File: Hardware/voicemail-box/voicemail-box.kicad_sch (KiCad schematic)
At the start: 6 parts, among them J101 Conn_02x08_Odd_Even, J102 Conn_02x03_Odd_Even, J103 Conn_02x08_Odd_Even

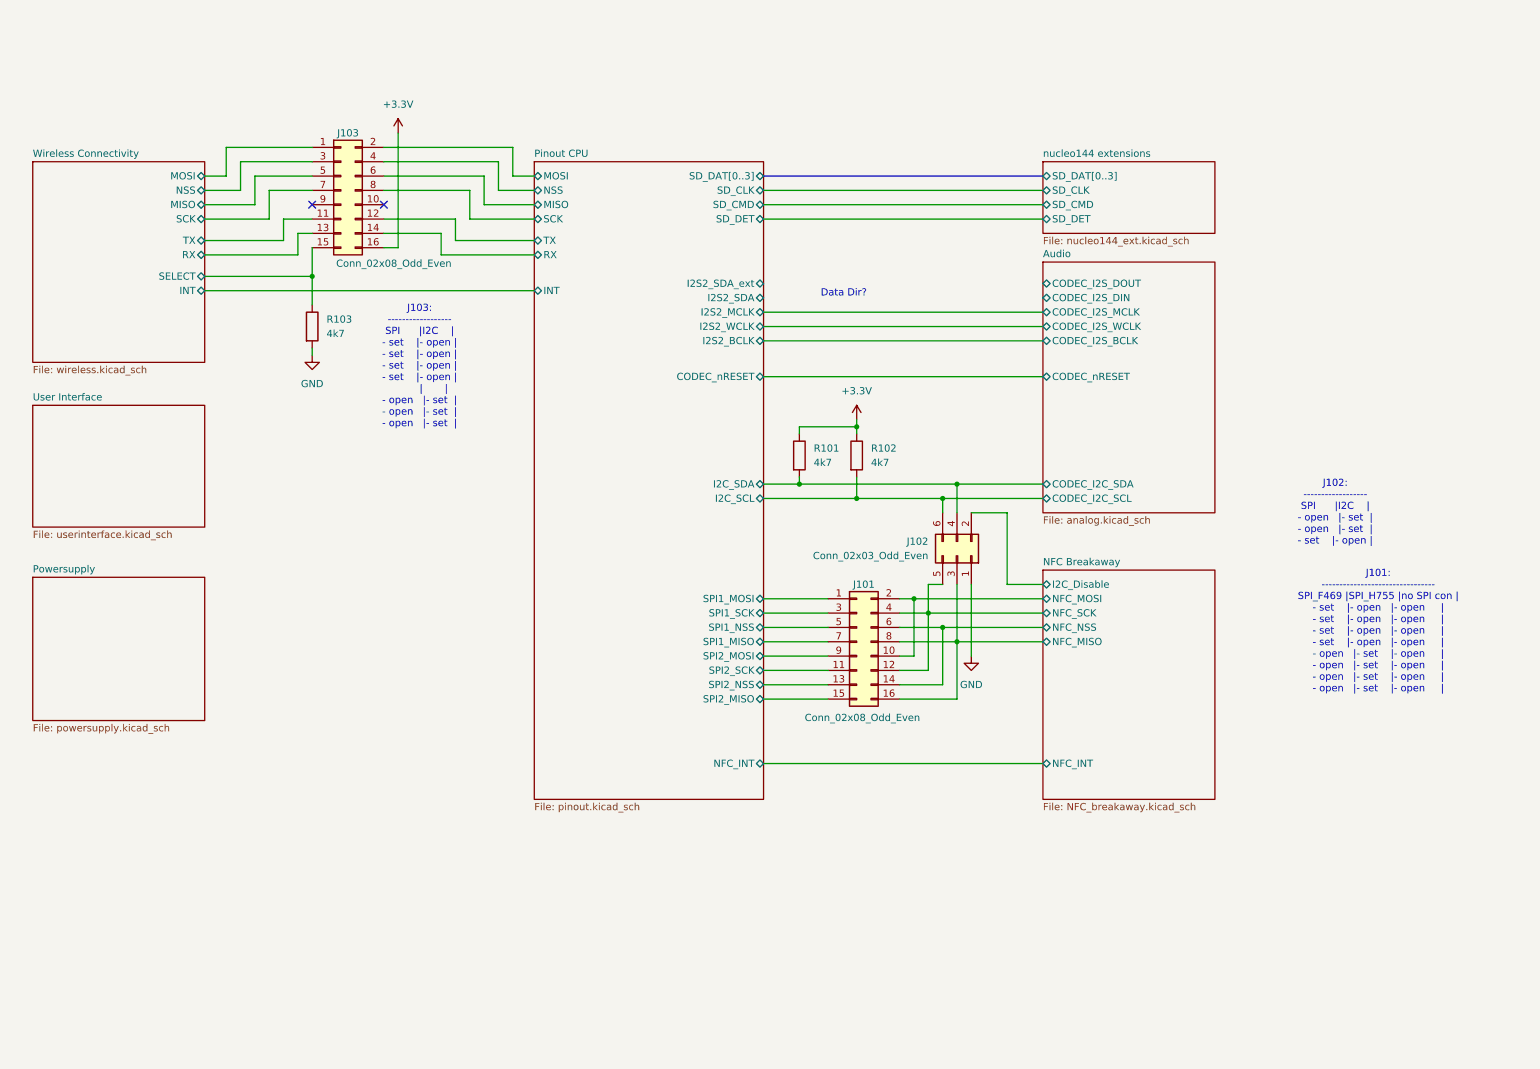
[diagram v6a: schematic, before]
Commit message: HW Layout progress todo: + Antenna + Audio Jacks + Planes (Supply only)
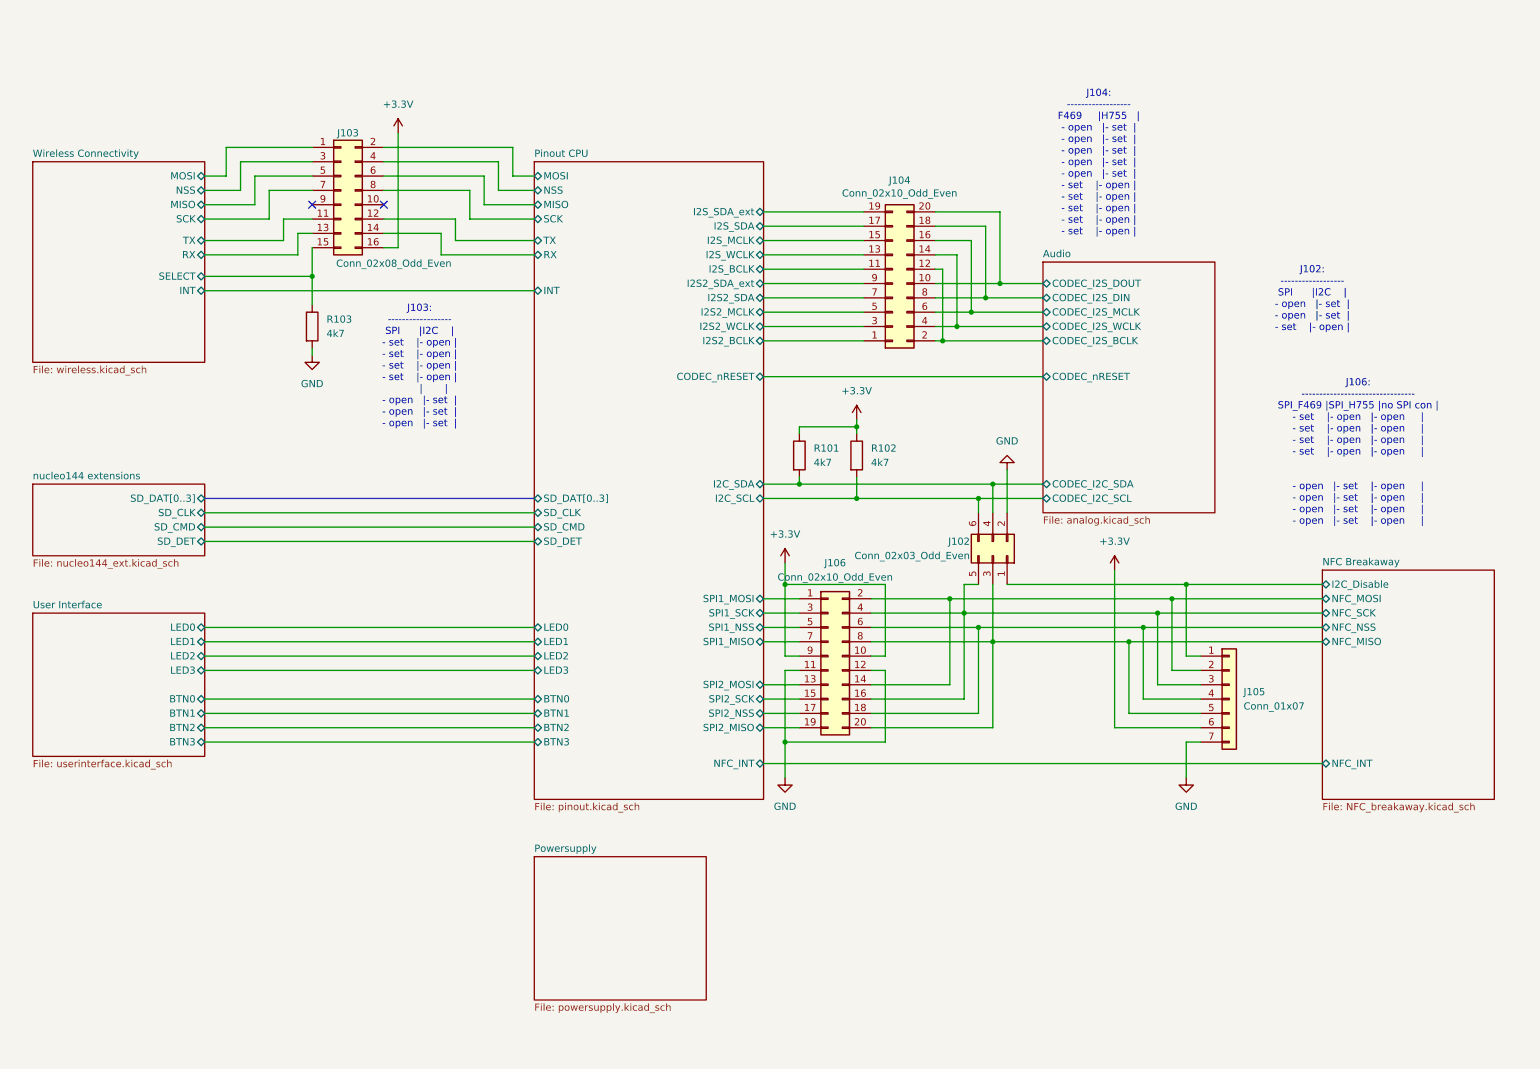
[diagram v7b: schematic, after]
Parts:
- removed J101: Conn_02x08_Odd_Even, Connector_PinHeader_2.54mm:PinHeader_2x08_P2.54mm_Vertical, symbol Connector_Generic:Conn_02x08_Odd_Even
- added J104, J106: Conn_02x10_Odd_Even, Connector_PinHeader_2.54mm:PinHeader_2x10_P2.54mm_Vertical, symbol Connector_Generic:Conn_02x10_Odd_Even
- added J105: Conn_01x07, Connector_PinHeader_2.54mm:PinHeader_1x07_P2.54mm_Vertical, symbol Connector_Generic:Conn_01x07
- J102: footprint Connector_PinSocket_2.54mm:PinSocket_2x03_P2.54mm_Vertical -> Connector_PinHeader_2.54mm:PinHeader_2x03_P2.54mm_Vertical
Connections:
- net +3.3V: now also J105.6 (Pin_6), J106.10 (Pin_10), J106.9 (Pin_9)
- net Audio/CODEC_I2S_BCLK: now also J104.12 (Pin_12), J104.2 (Pin_2)
- net Audio/CODEC_I2S_DIN: now also J104.18 (Pin_18), J104.8 (Pin_8)
- net Audio/CODEC_I2S_DOUT: now also J104.10 (Pin_10), J104.20 (Pin_20)
- net Audio/CODEC_I2S_MCLK: now also J104.16 (Pin_16), J104.6 (Pin_6)
- net Audio/CODEC_I2S_WCLK: now also J104.14 (Pin_14), J104.4 (Pin_4)
- net GND: now also J102.2 (Pin_2), J105.7 (Pin_7), J106.11 (Pin_11), J106.12 (Pin_12); no longer J102.1 (Pin_1)
- net NFC Breakaway/I2C_Disable: now also J102.1 (Pin_1), J105.1 (Pin_1); no longer J102.2 (Pin_2)
- net NFC Breakaway/NFC_MISO: now also J105.5 (Pin_5), J106.20 (Pin_20), J106.8 (Pin_8)
- net NFC Breakaway/NFC_MOSI: now also J105.2 (Pin_2), J106.14 (Pin_14), J106.2 (Pin_2)
- net NFC Breakaway/NFC_NSS: now also J105.4 (Pin_4), J106.18 (Pin_18), J106.6 (Pin_6)
- net NFC Breakaway/NFC_SCK: now also J105.3 (Pin_3), J106.16 (Pin_16), J106.4 (Pin_4)
- net Pinout CPU/I2S2_SDA: now also J104.7 (Pin_7)
- net Pinout CPU/I2S2_SDA_ext: now also J104.9 (Pin_9)
- net Pinout CPU/SPI1_MISO: now also J106.7 (Pin_7)
- net Pinout CPU/SPI1_MOSI: now also J106.1 (Pin_1)
- net Pinout CPU/SPI1_NSS: now also J106.5 (Pin_5)
- net Pinout CPU/SPI1_SCK: now also J106.3 (Pin_3)
- net Pinout CPU/SPI2_MISO: now also J106.19 (Pin_19)
- net Pinout CPU/SPI2_MOSI: now also J106.13 (Pin_13)
- net Pinout CPU/SPI2_NSS: now also J106.17 (Pin_17)
- net Pinout CPU/SPI2_SCK: now also J106.15 (Pin_15)
- new net Pinout CPU/I2S2_BCLK: J104.1 (Pin_1)
- new net Pinout CPU/I2S2_MCLK: J104.5 (Pin_5)
- new net Pinout CPU/I2S2_WCLK: J104.3 (Pin_3)
- new net Pinout CPU/I2S_BCLK: J104.11 (Pin_11)
- new net Pinout CPU/I2S_MCLK: J104.15 (Pin_15)
- new net Pinout CPU/I2S_SDA: J104.17 (Pin_17)
- new net Pinout CPU/I2S_SDA_ext: J104.19 (Pin_19)
- new net Pinout CPU/I2S_WCLK: J104.13 (Pin_13)
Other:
- sheet Pinout CPU ports: added BTN0, BTN1, BTN2, BTN3, I2S_BCLK, I2S_MCLK, I2S_SDA, I2S_SDA_ext, I2S_WCLK, LED0, LED1, LED2, LED3; removed none
- sheet User Interface ports: added BTN0, BTN1, BTN2, BTN3, LED0, LED1, LED2, LED3; removed none
- note added: "J104: ------------------ F469 |H755 | - open |- set | - open |- set | - open |- set | - open |- set | - open |- set | - set |- open | - set |- open | - set |- open | - set |- open | - set |- open |"
- note added: "J106: -------------------------------- SPI_F469 |SPI_H755 |no SPI con | - set |- open |- open | - set |- open |- open | - set |- open |- open | - set |- open |- open | - open |- set |- open | - open |- set |- open | - open |- set |- open | - open |- set |- open |"
- note removed: "Data Dir?"
- note removed: "J101: -------------------------------- SPI_F469 |SPI_H755 |no SPI con | - set |- open |- open | - set |- open |- open | - set |- open |- open | - set |- open |- open | - open |- set |- open | - open |- set |- open | - open |- set |- open | - open |- set |- open |"
- moved on the sheet: J102

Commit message: layout progress step
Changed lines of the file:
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@@
 	(sheet
 		(at 20.32 119.38)
-		(size 30.48 25.4)
+		(size 30.48 41.91)
 		(exclude_from_sim no)
 		(in_bom yes)
@@
 		)
 		(property "Sheetfile" "userinterface.kicad_sch"
-			(at 20.32 145.3646 0)
+			(at 20.32 161.8746 0)
 			(effects
 				(font
@@
 	(sheet
 		(at 109.22 39.37)
-		(size 40.64 113.03)
+		(size 40.64 121.92)
 		(exclude_from_sim no)
 		(in_bom yes)
@@
 		)
 		(property "Sheetfile" "pinout.kicad_sch"
-			(at 109.22 152.9846 0)
+			(at 109.22 161.8746 0)
 			(effects
 				(font
@@
 	)
 	(sheet
-		(at 109.22 162.56)
+		(at 20.32 167.64)
 		(size 30.48 25.4)
 		(exclude_from_sim no)
@@
 		)
 		(property "Sheetname" "Powersupply"
-			(at 109.22 161.8484 0)
+			(at 20.32 166.9284 0)
 			(effects
 				(font
@@
 		)
 		(property "Sheetfile" "powersupply.kicad_sch"
-			(at 109.22 188.5446 0)
-			(effects
-				(font
+			(at 20.32 193.6246 0)
+			(effects
+				(font
